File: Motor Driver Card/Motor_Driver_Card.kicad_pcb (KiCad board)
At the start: 2 copper layers, 129.5 x 76.8 mm, 37 parts, among them M1 MD13B, M2 MD13B, M3 MD13B, M4 MD13B, Q1 2N3904, Q2 2N3904, Q3 2N3904, Q4 2N3904

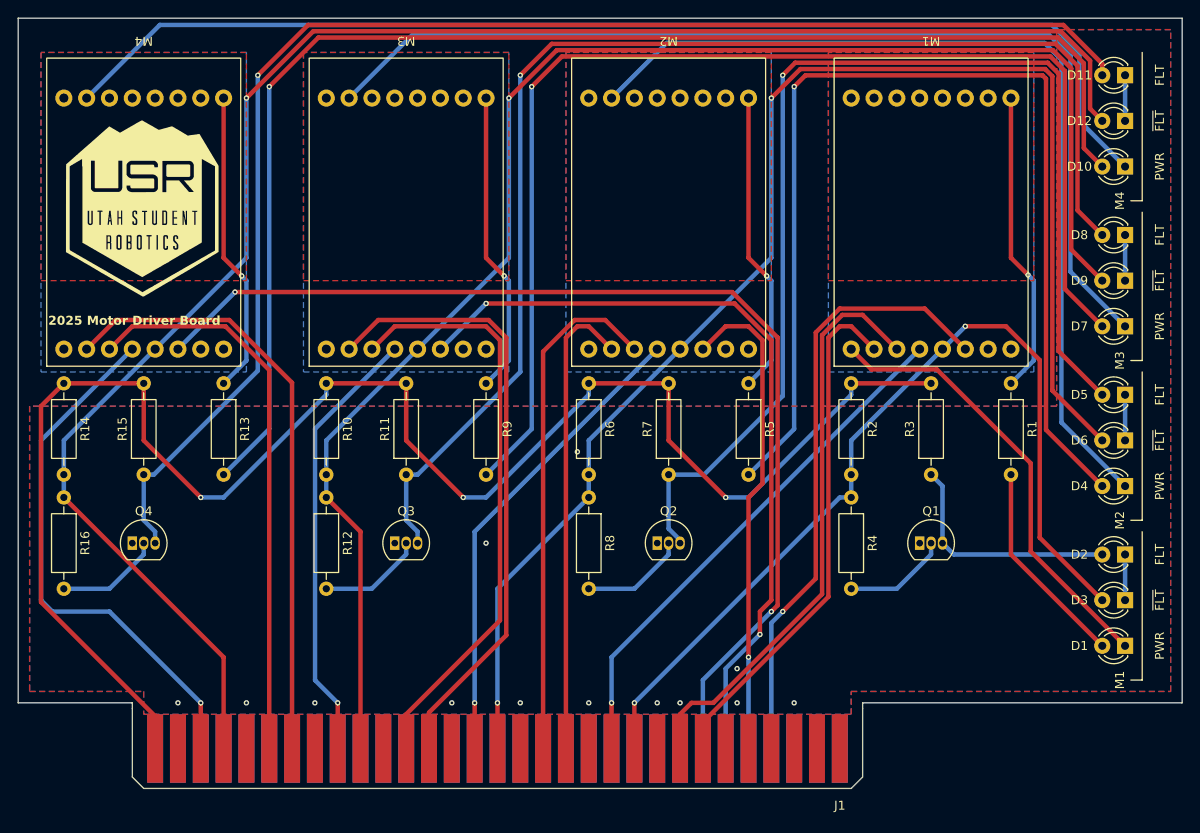
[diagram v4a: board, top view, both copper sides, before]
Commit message: Add thermistors to motor driver card
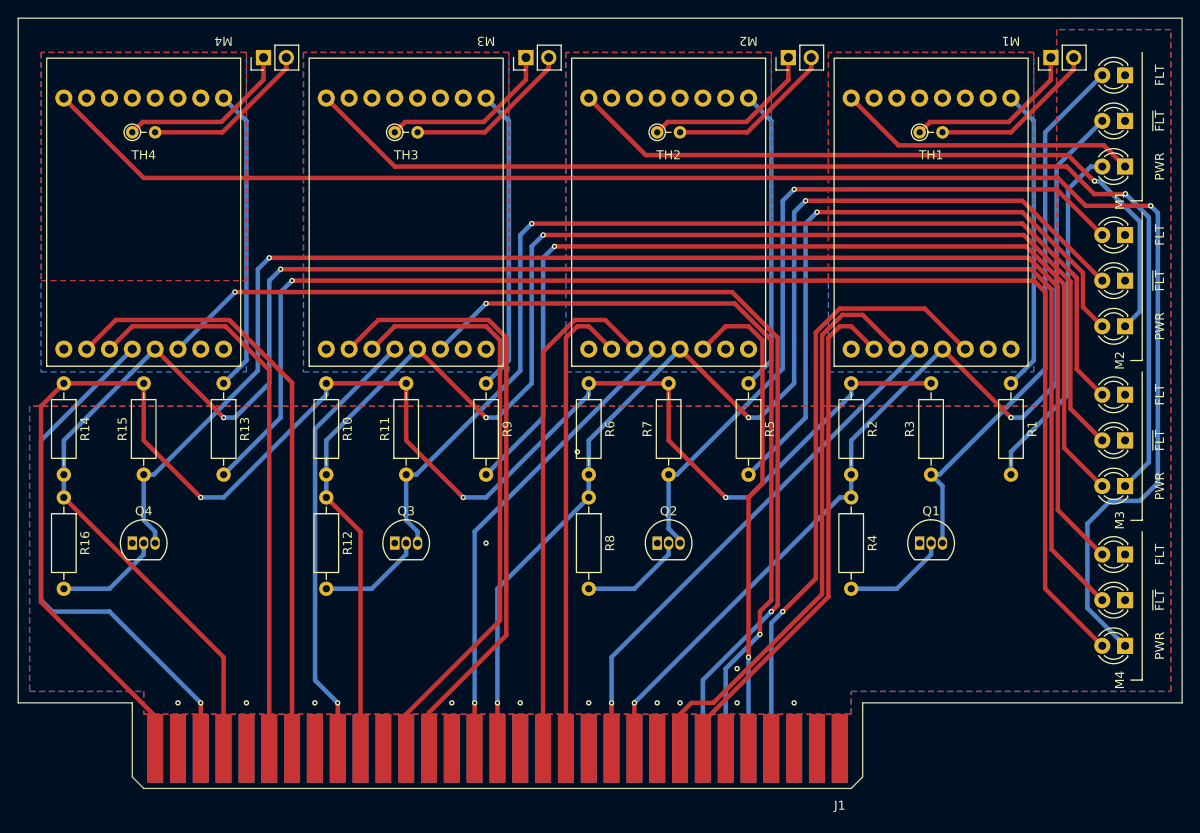
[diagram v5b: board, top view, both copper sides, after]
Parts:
- added J2: JST, Connector_PinHeader_2.54mm:PinHeader_1x02_P2.54mm_Vertical, F.Cu at (221.6, 59.0)
- added J3: JST, Connector_PinHeader_2.54mm:PinHeader_1x02_P2.54mm_Vertical, F.Cu at (192.4, 59.0)
- added J4: JST, Connector_PinHeader_2.54mm:PinHeader_1x02_P2.54mm_Vertical, F.Cu at (163.2, 59.0)
- added J5: JST, Connector_PinHeader_2.54mm:PinHeader_1x02_P2.54mm_Vertical, F.Cu at (134.0, 59.0)
- added TH1: Thermistor_US, Resistor_THT:R_Axial_DIN0204_L3.6mm_D1.6mm_P2.54mm_Vertical, F.Cu at (207.0, 67.3)
- added TH2: Thermistor_US, Resistor_THT:R_Axial_DIN0204_L3.6mm_D1.6mm_P2.54mm_Vertical, F.Cu at (177.8, 67.3)
- added TH3: Thermistor_US, Resistor_THT:R_Axial_DIN0204_L3.6mm_D1.6mm_P2.54mm_Vertical, F.Cu at (148.6, 67.3)
- added TH4: Thermistor_US, Resistor_THT:R_Axial_DIN0204_L3.6mm_D1.6mm_P2.54mm_Vertical, F.Cu at (119.4, 67.3)
- moved D11 53.3 mm to (229.9, 114.3)
- moved D2 53.3 mm to (229.9, 61.0)
- moved D1 53.3 mm to (229.9, 71.1)
- moved D10 53.3 mm to (229.9, 124.5)
- moved D12 53.3 mm to (229.9, 119.4)
- moved D3 53.3 mm to (229.9, 66.0)
- moved D4 17.8 mm to (229.9, 88.9)
- moved D5 17.8 mm to (229.9, 78.7)
- moved D6 17.8 mm to (229.9, 83.8)
- moved D7 17.8 mm to (229.9, 106.7)
- moved D8 17.8 mm to (229.9, 96.5)
- moved D9 17.8 mm to (229.9, 101.6)
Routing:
- net Net-(D10-K): track 129.9 -> 182.2 mm, vias 0 -> 1
- net Net-(D4-A): track 121.9 -> 71.6 mm
- net Net-(D5-A): track 129.7 -> 82.6 mm
- net Net-(D2-A): track 26.5 -> 61.0 mm
- net /FLT2: track 160.8 -> 127.8 mm, vias 2 -> 3
- net Net-(D7-A): track 136.8 -> 111.2 mm
- net Net-(D4-K): track 103.8 -> 79.4 mm, vias 0 -> 1
- net Net-(D8-A): track 143.0 -> 119.9 mm
- net GND: track 20.3 -> 0.00 mm
- net Net-(J2-Pin_1): track 0.00 -> 19.5 mm
- net Net-(J3-Pin_1): track 0.00 -> 19.5 mm
- net Net-(J5-Pin_1): track 0.00 -> 19.5 mm
- net Net-(J4-Pin_1): track 0.00 -> 19.5 mm
- net Net-(J2-Pin_2): track 0.00 -> 18.8 mm
- net Net-(J5-Pin_2): track 0.00 -> 18.7 mm
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
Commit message: Changed 2025 to 2026 on motor driver silkscreen. Motor driver card is now considered complete.
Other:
- board text added: "2026 Motor Driver Board"
- board text removed: "2025 Motor Driver Board"
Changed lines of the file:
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@@
 		)
 	)
-	(gr_text "2025 Motor Driver Board"
-		(at 141.9713 130.2214 -0)
+	(gr_text "2026 Motor Driver Board"
+		(at 141.9713 130.2214 0)
 		(layer "B.SilkS")
 		(effects
@@
 			(keep_text_aligned yes)
 		)
-		(gr_text "5100"
+		(gr_text "129.54"
 			(at 171.45 38.84 0)
 			(layer "F.Cu")
@@
 			(keep_text_aligned yes)
 		)
-		(gr_text "3000"
+		(gr_text "76.2"
 			(at 252.2 92.71 90)
 			(layer "F.Cu")

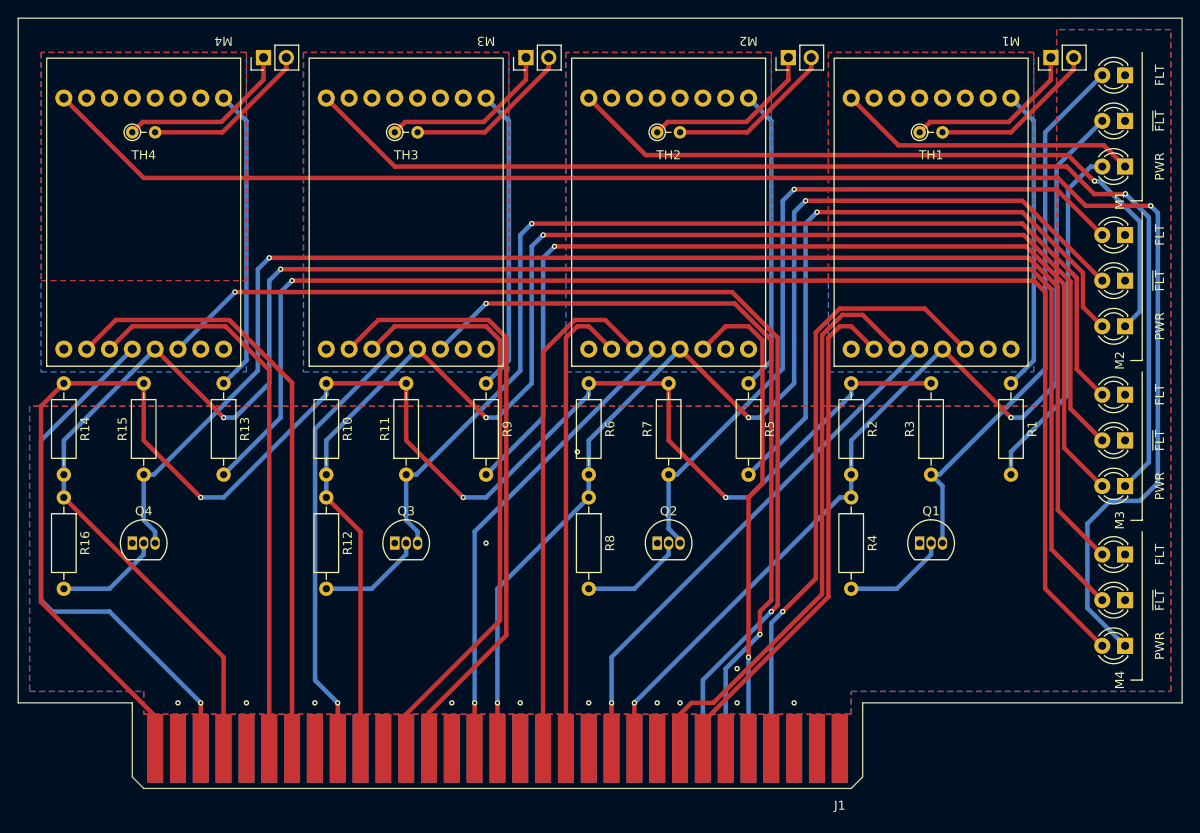
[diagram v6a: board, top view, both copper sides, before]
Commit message: Finalized designs for MCU card, Analog board, and MDCB
Added additional vias to all in order to minimize ground loops and stitch together front and back ground planes.
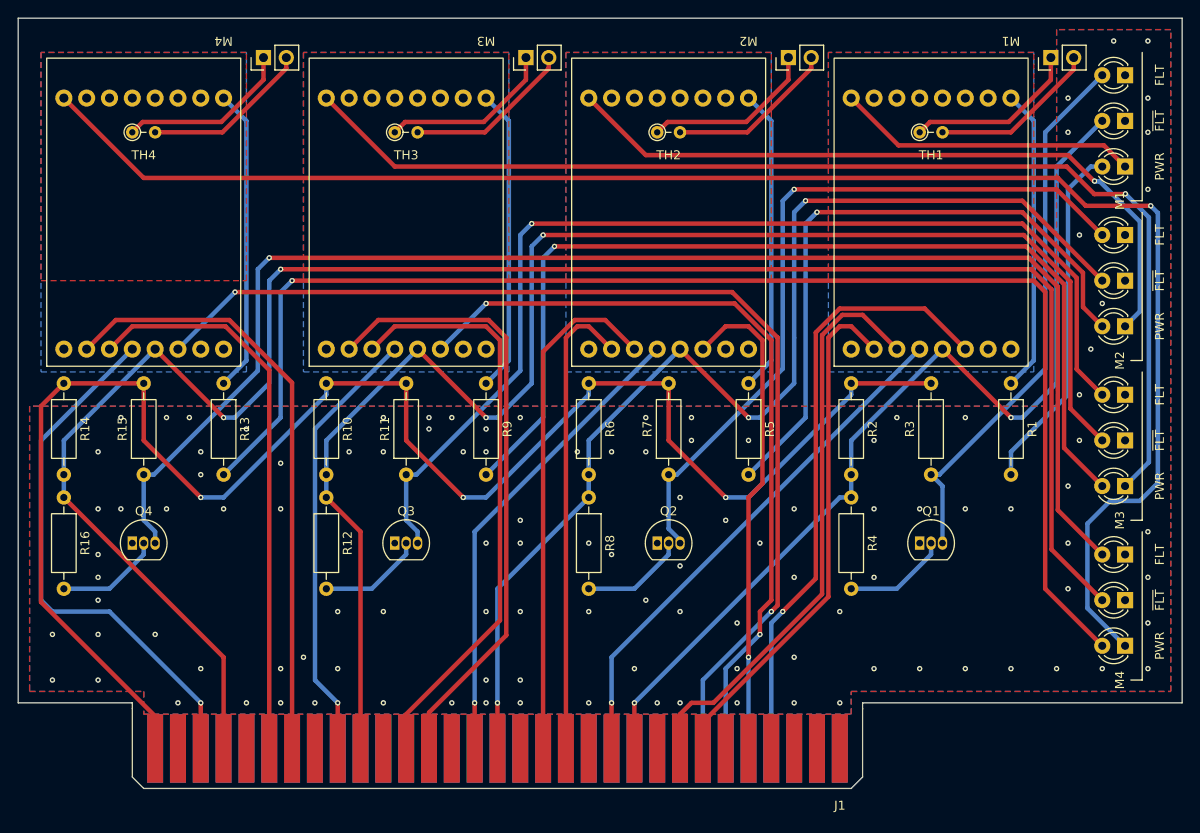
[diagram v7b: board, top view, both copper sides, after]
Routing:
- net GND: vias 13 -> 112
- net (no net): vias 0 -> 2

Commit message: Last-minute changes for pico GPIO voltage levels
Adjusted MDCB to work in 3.3v rather than 5v to not blow up a pico. Thankfully we have a readily available 3.3v source from the motor drivers themselves.
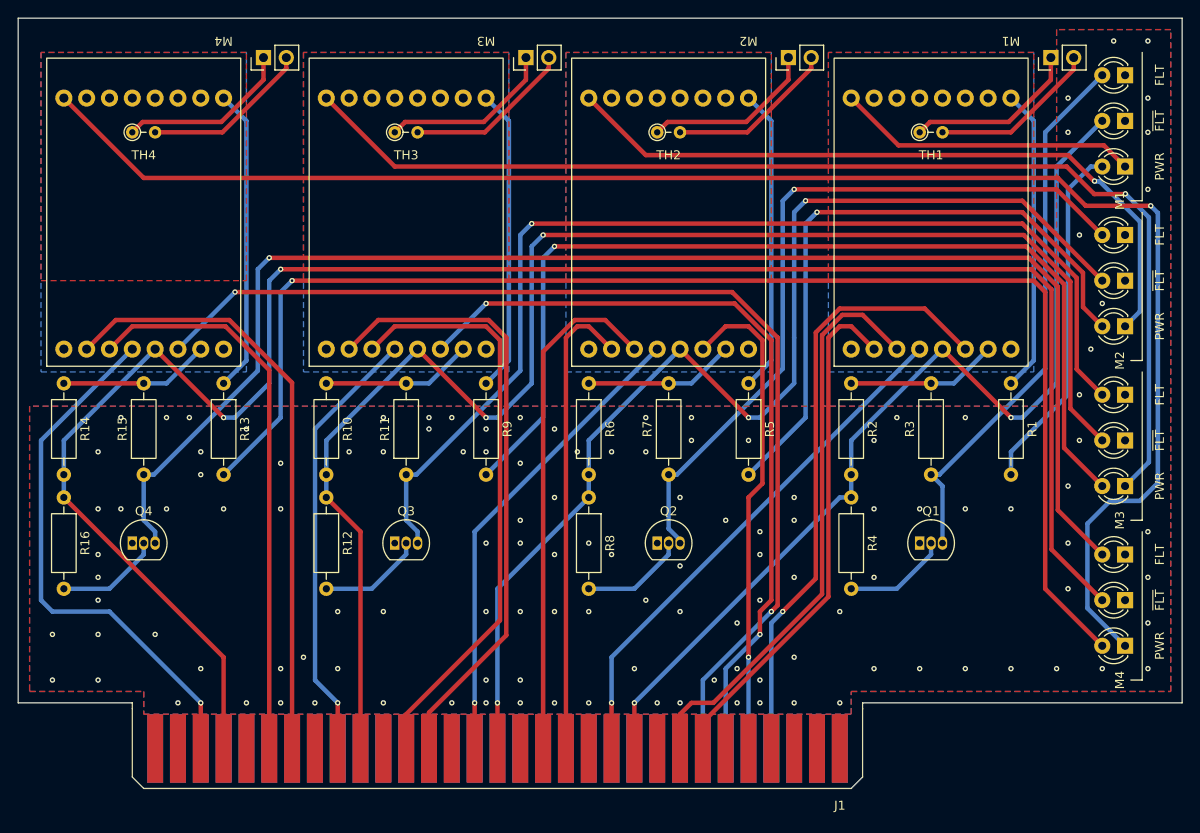
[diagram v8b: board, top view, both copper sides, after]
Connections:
- M1 pad 8: unconnected-(M1-3V3-Pad8) -> Net-(M1-3V3)
- M2 pad 8: unconnected-(M2-3V3-Pad8) -> Net-(M2-3V3)
- M3 pad 8: unconnected-(M3-3V3-Pad8) -> Net-(M3-3V3)
- M4 pad 8: unconnected-(M4-3V3-Pad8) -> Net-(M4-3V3)
- R10 pad 1: +5V -> Net-(M3-3V3)
- R11 pad 2: +5V -> Net-(M3-3V3)
- R14 pad 1: +5V -> Net-(M4-3V3)
- R15 pad 2: +5V -> Net-(M4-3V3)
- R2 pad 1: +5V -> Net-(M1-3V3)
- R3 pad 2: +5V -> Net-(M1-3V3)
- R6 pad 1: +5V -> Net-(M2-3V3)
- R7 pad 2: +5V -> Net-(M2-3V3)
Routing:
- net +5V: track 188.4 -> 3.60 mm, vias 3 -> 0
- net Net-(M3-3V3): track 0.00 -> 16.8 mm
- net Net-(M1-3V3): track 0.00 -> 16.8 mm
- net Net-(M4-3V3): track 0.00 -> 16.8 mm
- net Net-(M2-3V3): track 0.00 -> 16.8 mm
- net GND: vias 112 -> 126
- net (no net): vias 2 -> 0
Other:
- board text added: "JG VB"
